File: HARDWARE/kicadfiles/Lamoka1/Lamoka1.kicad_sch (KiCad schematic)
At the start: 0 parts

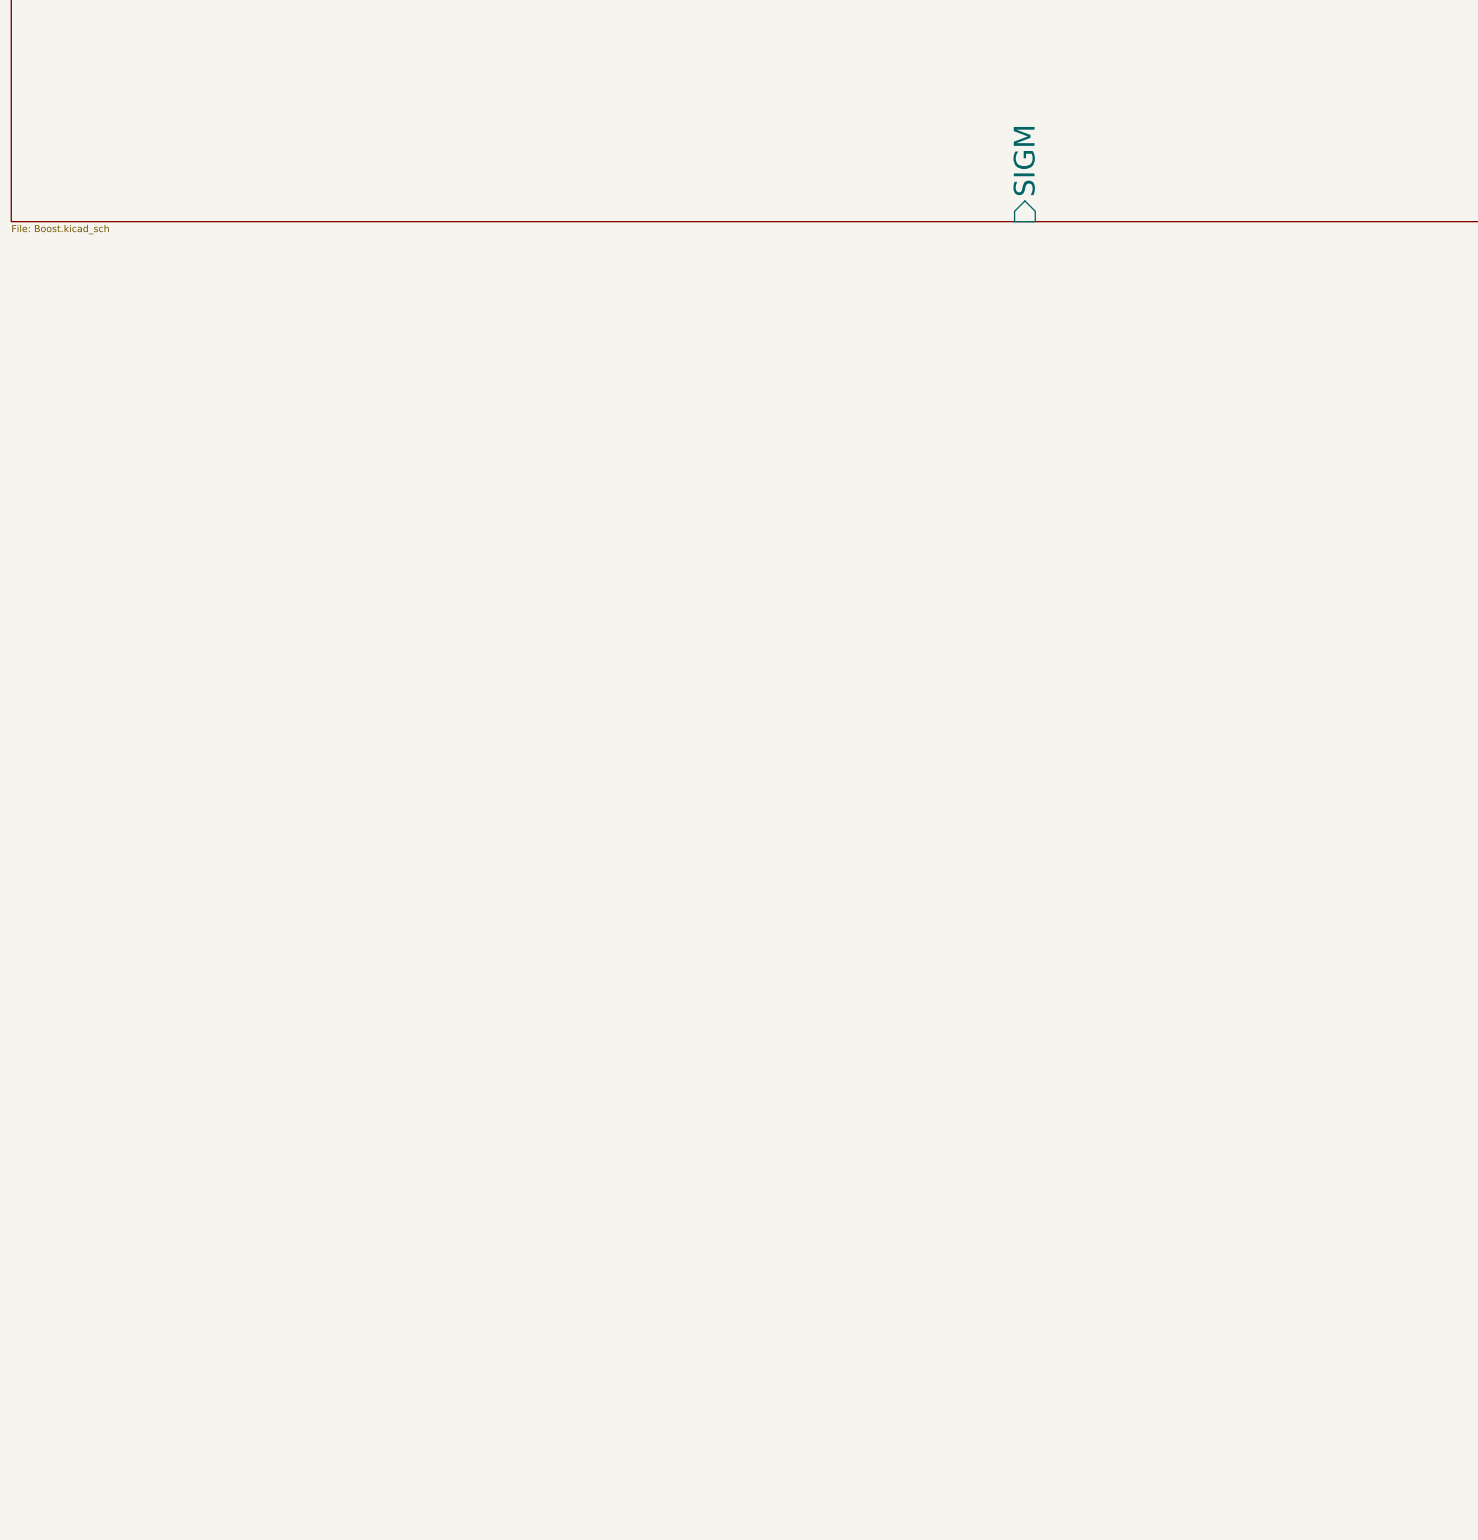
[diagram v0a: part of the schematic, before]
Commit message: ADD charging section and multiple color Dev-Brain 3d print
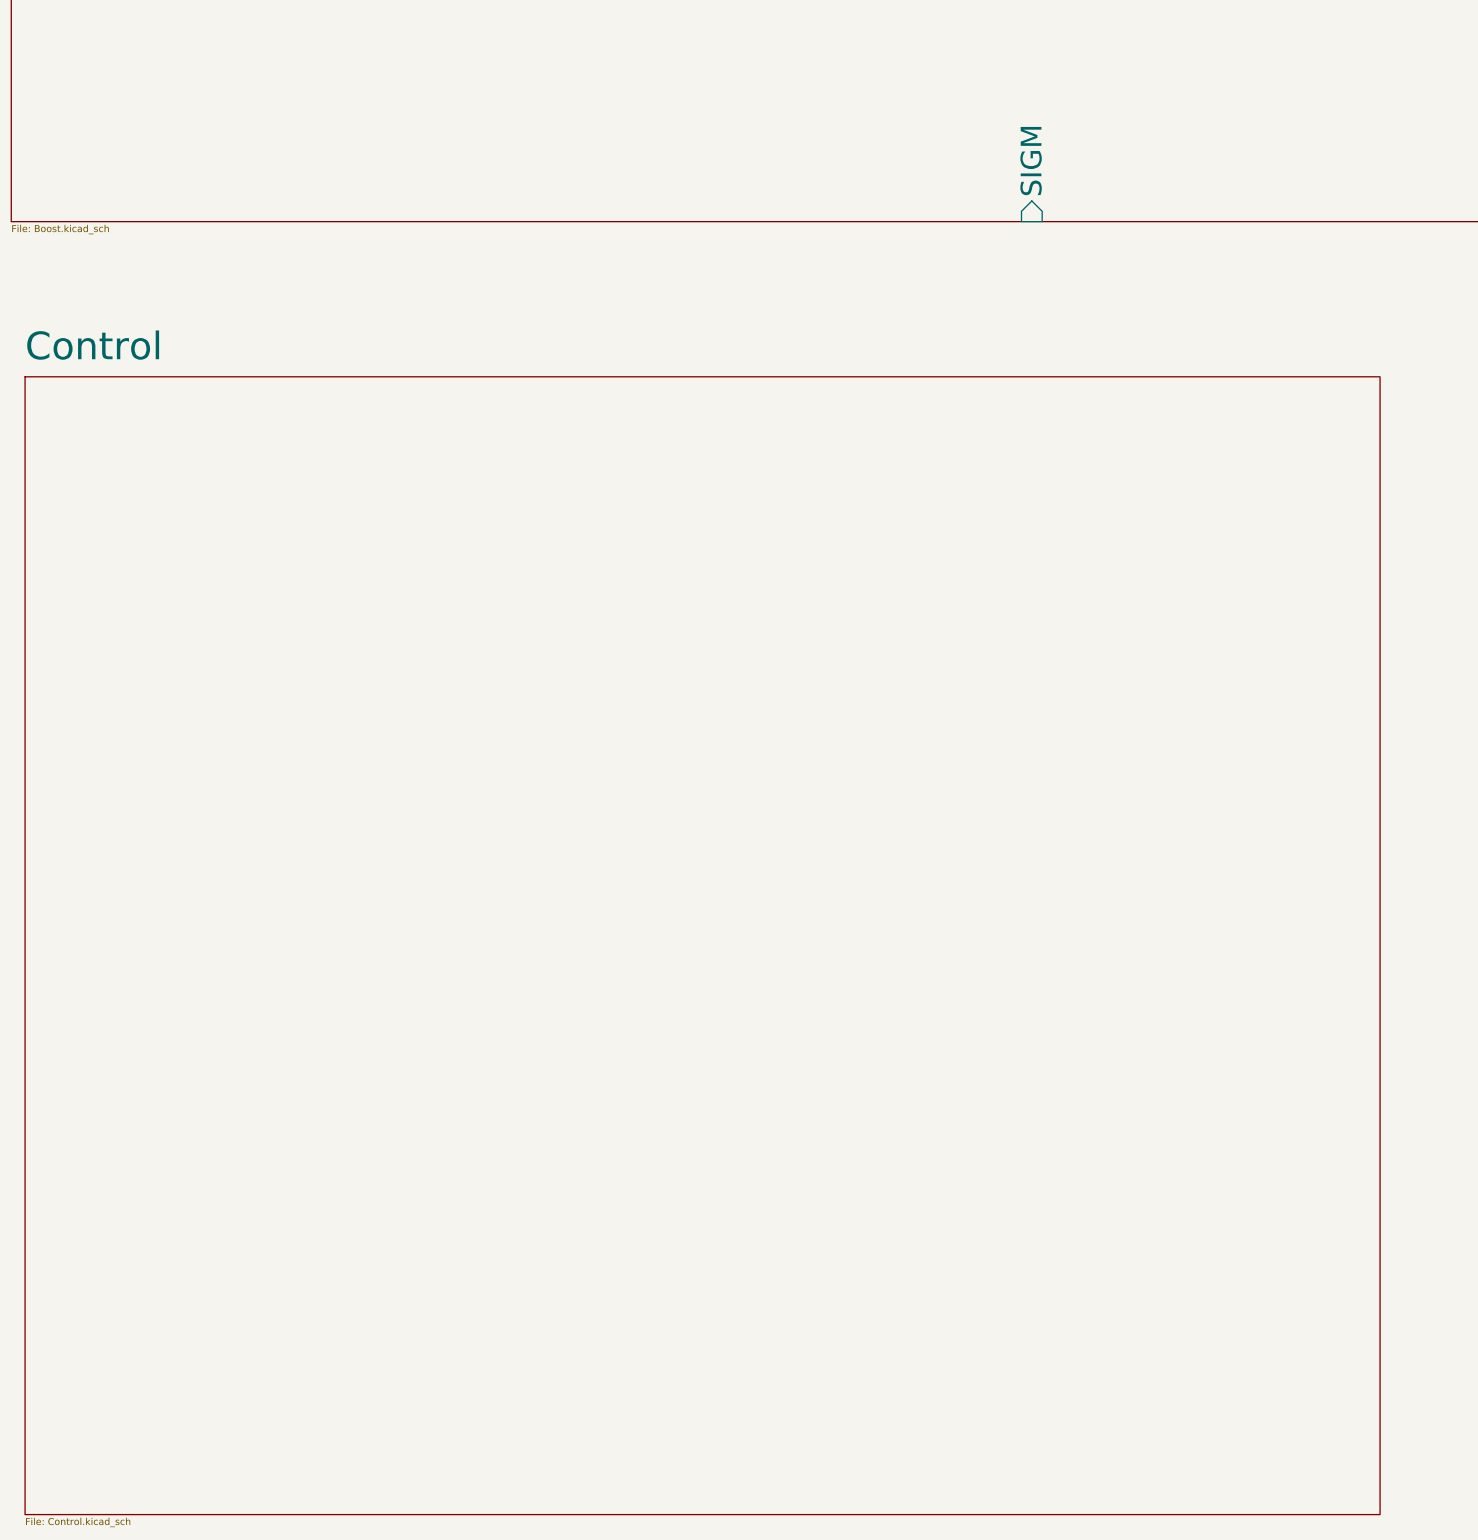
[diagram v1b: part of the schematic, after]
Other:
- added sheet Control (Control.kicad_sch)
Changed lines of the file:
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@@
 		)
 		(pin "SIGM" input
-			(at 213.36 256.54 270)
+			(at 214.63 256.54 270)
 			(effects
 				(font
@@
 				)
 			)
+		)
+	)
+	(sheet
+		(at 29.21 285.115)
+		(size 249.555 209.55)
+		(exclude_from_sim no)
+		(in_bom yes)
+		(on_board yes)
+		(dnp no)
+		(fields_autoplaced yes)
+		(stroke
+			(width 0.1524)
+			(type solid)
+		)
+		(fill
+			(color 0 0 0 0)
+		)
+		(property "Sheetname" "Control"
+			(at 29.21 282.4984 0)
+			(show_name no)
+			(do_not_autoplace no)
+			(effects
+				(font
+					(size 5.08 5.08)
+				)
+				(justify left bottom)
+			)
+		)
+		(property "Sheetfile" "Control.kicad_sch"
+			(at 29.21 495.2496 0)
+			(show_name no)
+			(do_not_autoplace no)
+			(effects
+				(font
+					(size 1.27 1.27)
+				)
+				(justify left top)
+			)
+		)
+		(instances
+			(project "Lamoka1"
+				(path "/50fe8bbc-b3f6-4de5-9677-9b5870b87390"
+					(page "4")
+				)
+			)

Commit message: re connect control
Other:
- sheet Charging Section ports: added 3v3, CHG_CE, CHG_INT, I2C_SCL, I2C_SDA, VIN-SOURCE; removed none
- sheet Control ports: added CHG_CE, CHG_INT, I2C_SCL, I2C_SDA, SIGM; removed none
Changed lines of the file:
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@@
 	(generator_version "10.0")
 	(paper "User" 762 762)
+	(wire
+		(pts
+			(xy 280.67 344.17) (xy 384.81 344.17)
+		)
+		(stroke
+			(width 0)
+			(type default)
+		)
+	)
+	(wire
+		(pts
+			(xy 401.32 132.08) (xy 384.81 132.08)
+		)
+		(stroke
+			(width 0)
+			(type default)
+		)
+	)
+	(wire
+		(pts
+			(xy 401.32 139.7) (xy 386.08 139.7)
+		)
+		(stroke
+			(width 0)
+			(type default)
+		)
+	)
+	(wire
+		(pts
+			(xy 386.08 350.52) (xy 280.67 350.52)
+		)
+		(stroke
+			(width 0)
+			(type default)
+		)
+	)
+	(wire
+		(pts
+			(xy 384.81 132.08) (xy 384.81 344.17)
+		)
+		(stroke
+			(width 0)
+			(type default)
+		)
+	)
+	(wire
+		(pts
+			(xy 388.62 152.4) (xy 388.62 363.22)
+		)
+		(stroke
+			(width 0)
+			(type default)
+		)
+	)
+	(wire
+		(pts
+			(xy 388.62 363.22) (xy 280.67 363.22)
+		)
+		(stroke
+			(width 0)
+			(type default)
+		)
+	)
+	(wire
+		(pts
+			(xy 386.08 139.7) (xy 386.08 350.52)
+		)
+		(stroke
+			(width 0)
+			(type default)
+		)
+	)
+	(wire
+		(pts
+			(xy 401.32 152.4) (xy 388.62 152.4)
+		)
+		(stroke
+			(width 0)
+			(type default)
+		)
+	)
+	(wire
+		(pts
+			(xy 387.35 356.87) (xy 387.35 146.05)
+		)
+		(stroke
+			(width 0)
+			(type default)
+		)
+	)
+	(wire
+		(pts
+			(xy 387.35 146.05) (xy 401.32 146.05)
+		)
+		(stroke
+			(width 0)
+			(type default)
+		)
+	)
+	(wire
+		(pts
+			(xy 280.67 356.87) (xy 387.35 356.87)
+		)
+		(stroke
+			(width 0)
+			(type default)
+		)
+	)
 	(sheet
 		(at 26.67 24.13)
@@
 	)
 	(sheet
-		(at 29.21 285.115)
-		(size 249.555 209.55)
+		(at 29.21 286.258)
+		(size 251.46 208.407)
 		(exclude_from_sim no)
 		(in_bom yes)
@@
 		)
 		(property "Sheetname" "Control"
-			(at 29.21 282.4984 0)
+			(at 29.21 283.6414 0)
 			(show_name no)
 			(do_not_autoplace no)
@@
 				)
 				(justify left top)
+			)
+		)
+		(pin "CHG_CE" input
+			(at 280.67 363.22 0)
+			(effects
+				(font
+					(size 2.54 2.54)
+				)
+				(justify right)
+			)
+		)
+		(pin "CHG_INT" input
+			(at 280.67 356.87 0)
+			(effects
+				(font
+					(size 2.54 2.54)
+				)
+				(justify right)
+			)
+		)
+		(pin "I2C_SDA" input
+			(at 280.67 350.52 0)
+			(effects
+				(font
+					(size 2.54 2.54)
+				)
+				(justify right)
+			)
+		)
+		(pin "I2C_SCL" input
+			(at 280.67 344.17 0)
+			(effects
+				(font
+					(size 2.54 2.54)
+				)
+				(justify right)
+			)
+		)
+		(pin "SIGM" input
+			(at 280.67 369.57 0)
+			(effects
+				(font
+					(size 2.54 2.54)
+				)
+				(justify right)
 			)
 		)
@@
 			)
 		)
+		(pin "3v3" input
+			(at 401.32 191.77 180)
+			(effects
+				(font
+					(size 2.54 2.54)
+				)
+				(justify left)
+			)
+		)
+		(pin "CHG_CE" input
+			(at 401.32 152.4 180)
+			(effects
+				(font
+					(size 2.54 2.54)
+				)
+				(justify left)
+			)
+		)
+		(pin "CHG_INT" input
+			(at 401.32 146.05 180)
+			(effects
+				(font
+					(size 2.54 2.54)
+				)
+				(justify left)
+			)
+		)
+		(pin "I2C_SCL" input
+			(at 401.32 132.08 180)
+			(effects
+				(font
+					(size 2.54 2.54)
+				)
+				(justify left)
+			)
+		)
+		(pin "I2C_SDA" input
+			(at 401.32 139.7 180)
+			(effects
+				(font
+					(size 2.54 2.54)
+				)
+				(justify left)
+			)
+		)
+		(pin "VIN-SOURCE" input
+			(at 401.32 198.12 180)
+			(effects
+				(font
+					(size 2.54 2.54)
+				)
+				(justify left)
+			)
+		)
